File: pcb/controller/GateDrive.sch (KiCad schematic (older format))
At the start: 0 parts

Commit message: controller schematic capture almost done
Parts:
- added C? (x4): 10u, symbol Device:C
- added C? (x8): 0.1u, symbol Device:C
- added C? (x4): 1u, symbol Device:C
- added J? (x2): Conn_01x02_Female, symbol Connector:Conn_01x02_Female
- added Q? (x4): Q_NMOS_GSD, symbol Device:Q_NMOS_GSD
- added R? (x4): 10k, symbol Device:R
- added U? (x4): IXDD609D2, symbol wbraun_ic_lib:IXDD609D2
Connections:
- new net: C?.2, Q?.3 (D), R?.2, U?.3 (EN) (x4)
- new net: C?.2, C?.2, U?.6 (OUT), U?.7 (OUT) (x2)
- new net: J?.2 (Pin_2), U?.6 (OUT), U?.7 (OUT) (x2)
- new net: C?.1, C?.1, J?.1 (Pin_1) (x2)
- new net +24V: C?.1, C?.1, C?.1, C?.1, C?.1, C?.1, C?.1, C?.1, R?.1, R?.1, R?.1, R?.1, U?.1 (VCC), U?.1 (VCC), U?.1 (VCC), U?.1 (VCC), U?.8 (VCC), U?.8 (VCC), U?.8 (VCC), U?.8 (VCC)
- new net EN_1: Q?.1 (G)
- new net EN_2: Q?.1 (G)
- new net EN_3: Q?.1 (G)
- new net EN_4: Q?.1 (G)
- new net GATE_1: U?.2 (IN)
- new net GATE_2: U?.2 (IN)
- new net GATE_3: U?.2 (IN)
- new net GATE_4: U?.2 (IN)
- new net GND: C?.1, C?.1, C?.1, C?.1, C?.2, C?.2, C?.2, C?.2, C?.2, C?.2, C?.2, C?.2, Q?.2 (S), Q?.2 (S), Q?.2 (S), Q?.2 (S), U?.4 (GND), U?.4 (GND), U?.4 (GND), U?.4 (GND), U?.5 (GND), U?.5 (GND), U?.5 (GND), U?.5 (GND), U?.9 (EP), U?.9 (EP), U?.9 (EP), U?.9 (EP)

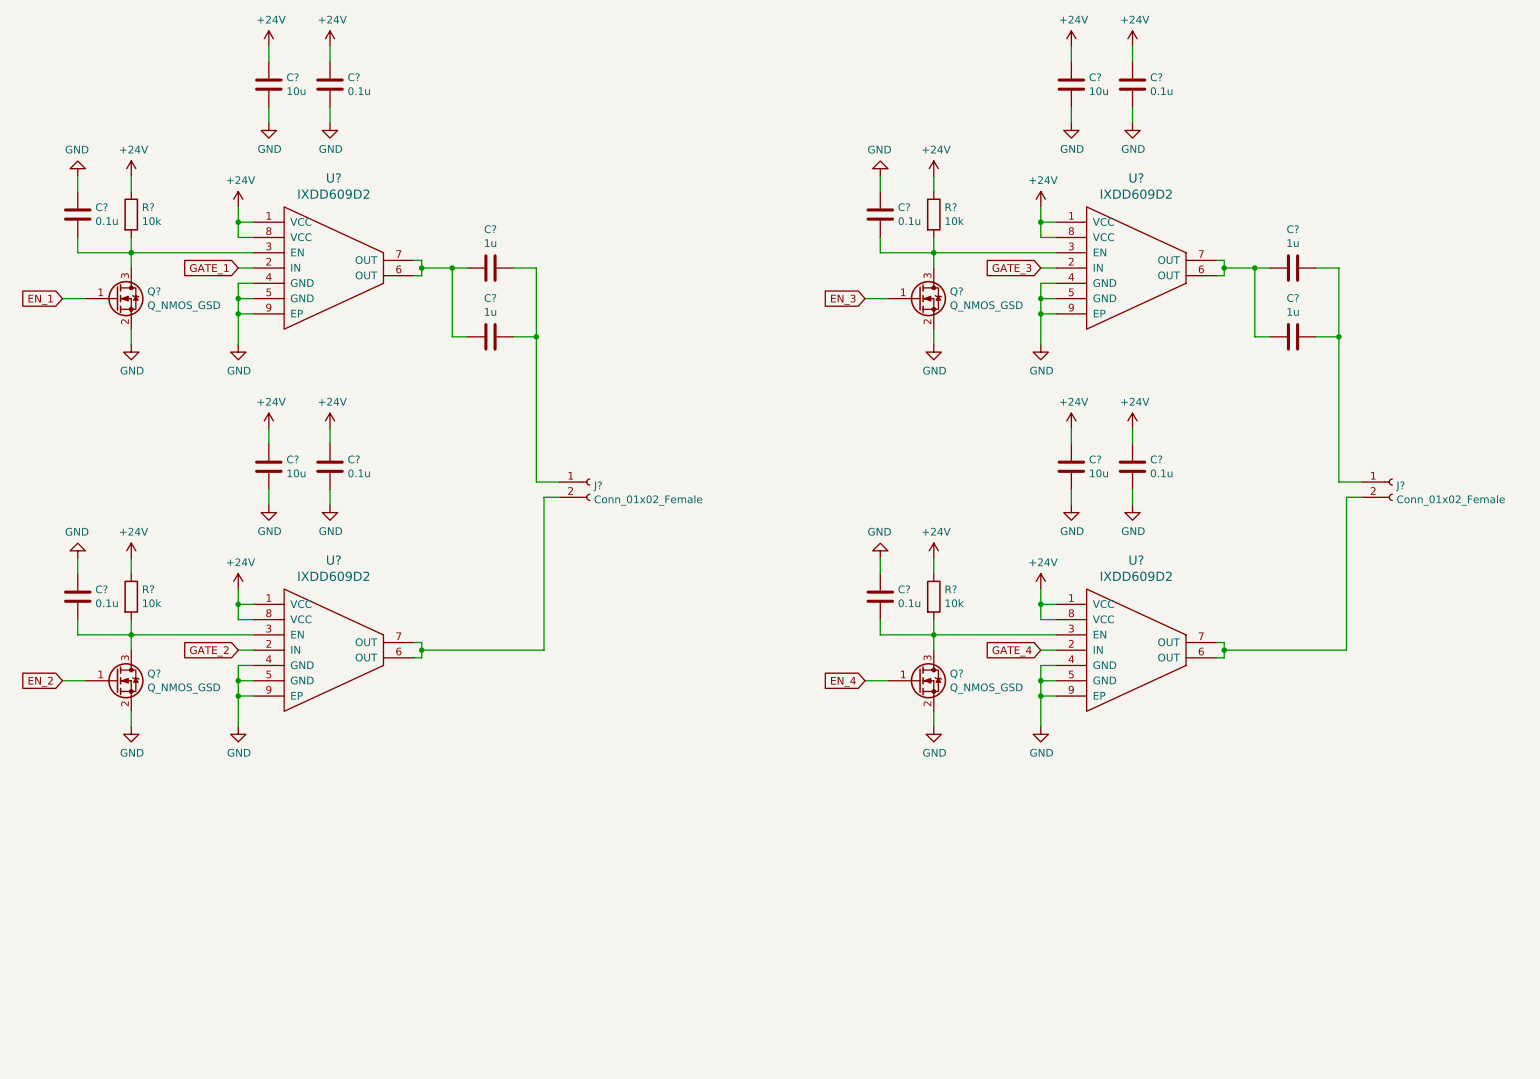
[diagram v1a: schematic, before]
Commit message: started assigning footprints
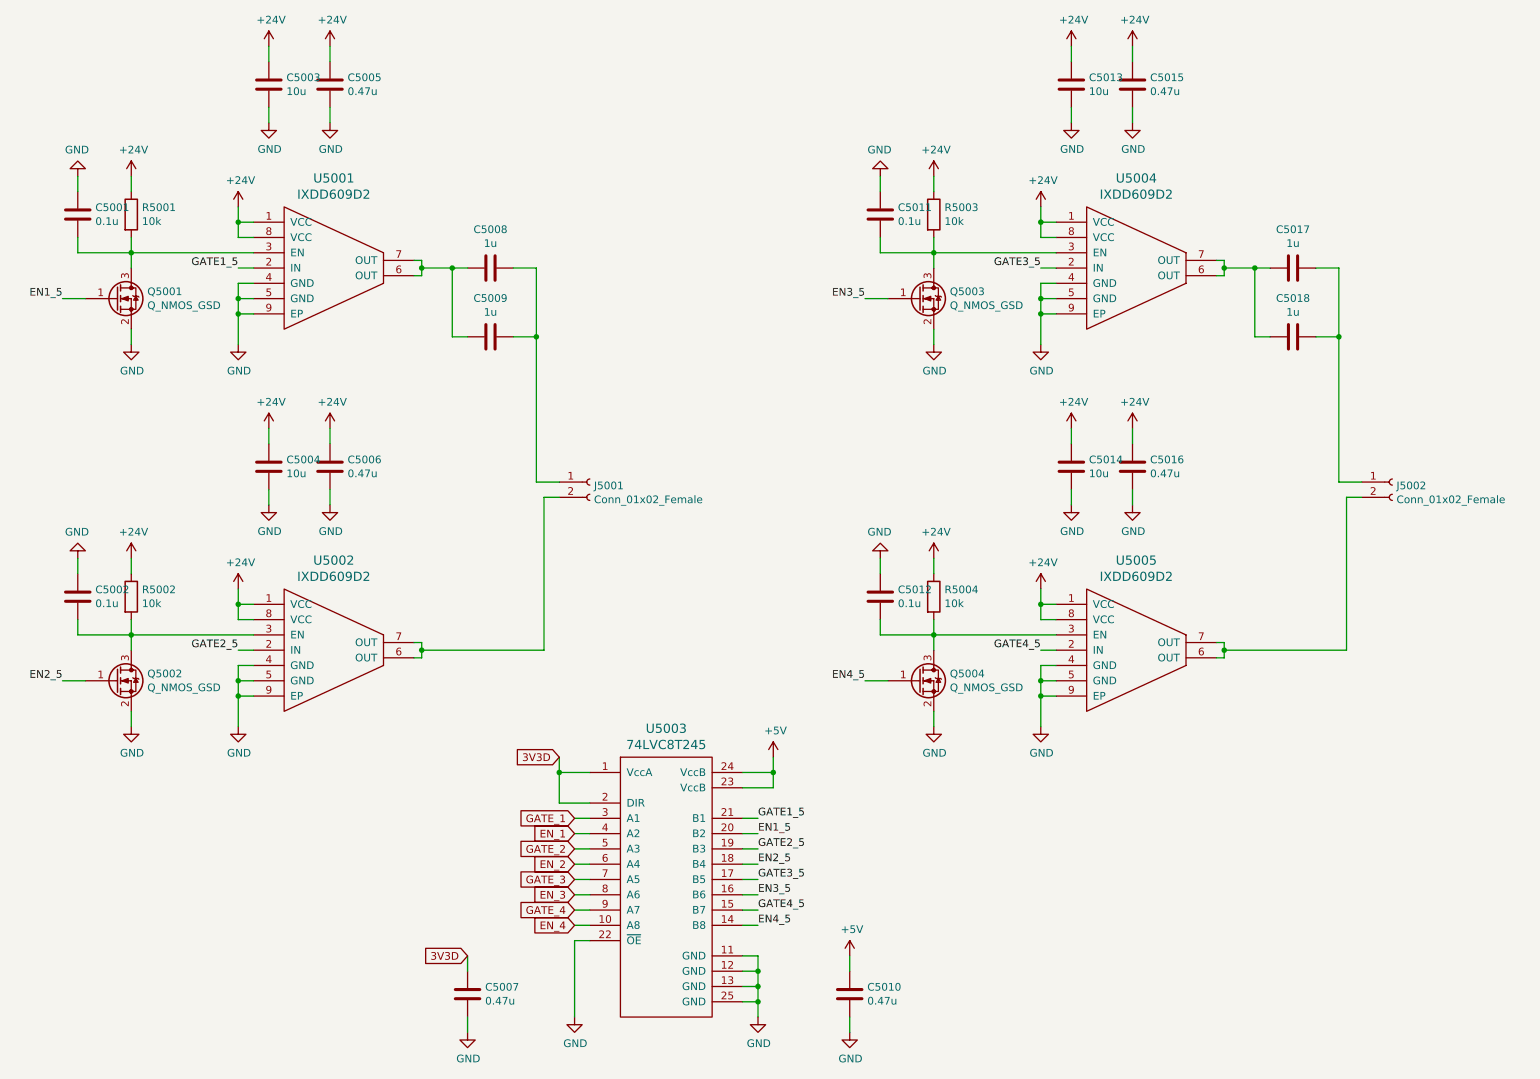
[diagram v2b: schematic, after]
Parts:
- added C5007, C5010: 0.47u, Capacitor_SMD:C_0402_1005Metric, symbol Device:C
- added U5003: 74LVC8T245, symbol wbraun_ic_lib:74LVC8T245
- C5001, C5002, C5008, C5009, C5011, C5012: renamed from C?; footprint (none) -> Capacitor_SMD:C_0805_2012Metric
- C5003, C5004, C5013: renamed from C?; footprint (none) -> Capacitor_SMD:C_1206_3216Metric
- C5005, C5006: renamed from C?; value 0.1u -> 0.47u; footprint (none) -> Capacitor_SMD:C_0805_2012Metric
- C5015, C5016: renamed from C?; value 0.1u -> 0.47u
- gave numbers to parts that had none: 17
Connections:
- net EN_1: now also U5003.4 (A2); no longer Q5001.1 (G)
- net EN_2: now also U5003.6 (A4); no longer Q5002.1 (G)
- net EN_3: now also U5003.8 (A6); no longer Q5003.1 (G)
- net EN_4: now also U5003.10 (A8); no longer Q5004.1 (G)
- net GATE_1: now also U5003.3 (A1); no longer U5001.2 (IN)
- net GATE_2: now also U5003.5 (A3); no longer U5002.2 (IN)
- net GATE_3: now also U5003.7 (A5); no longer U5004.2 (IN)
- net GATE_4: now also U5003.9 (A7); no longer U5005.2 (IN)
- net GND: now also C5007.2, C5010.2, U5003.11 (GND), U5003.12 (GND), U5003.13 (GND), U5003.22 (~OE), U5003.25 (GND)
- new net +5V: C5010.1, U5003.23 (VccB), U5003.24 (VccB)
- new net 3V3D: C5007.1, U5003.1 (VccA), U5003.2 (DIR)
- new net EN1_5: Q5001.1 (G), U5003.20 (B2)
- new net EN2_5: Q5002.1 (G), U5003.18 (B4)
- new net EN3_5: Q5003.1 (G), U5003.16 (B6)
- new net EN4_5: Q5004.1 (G), U5003.14 (B8)
- new net GATE1_5: U5001.2 (IN), U5003.21 (B1)
- new net GATE2_5: U5002.2 (IN), U5003.19 (B3)
- new net GATE3_5: U5003.17 (B5), U5004.2 (IN)
- new net GATE4_5: U5003.15 (B7), U5005.2 (IN)

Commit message: pcb component placement almost done
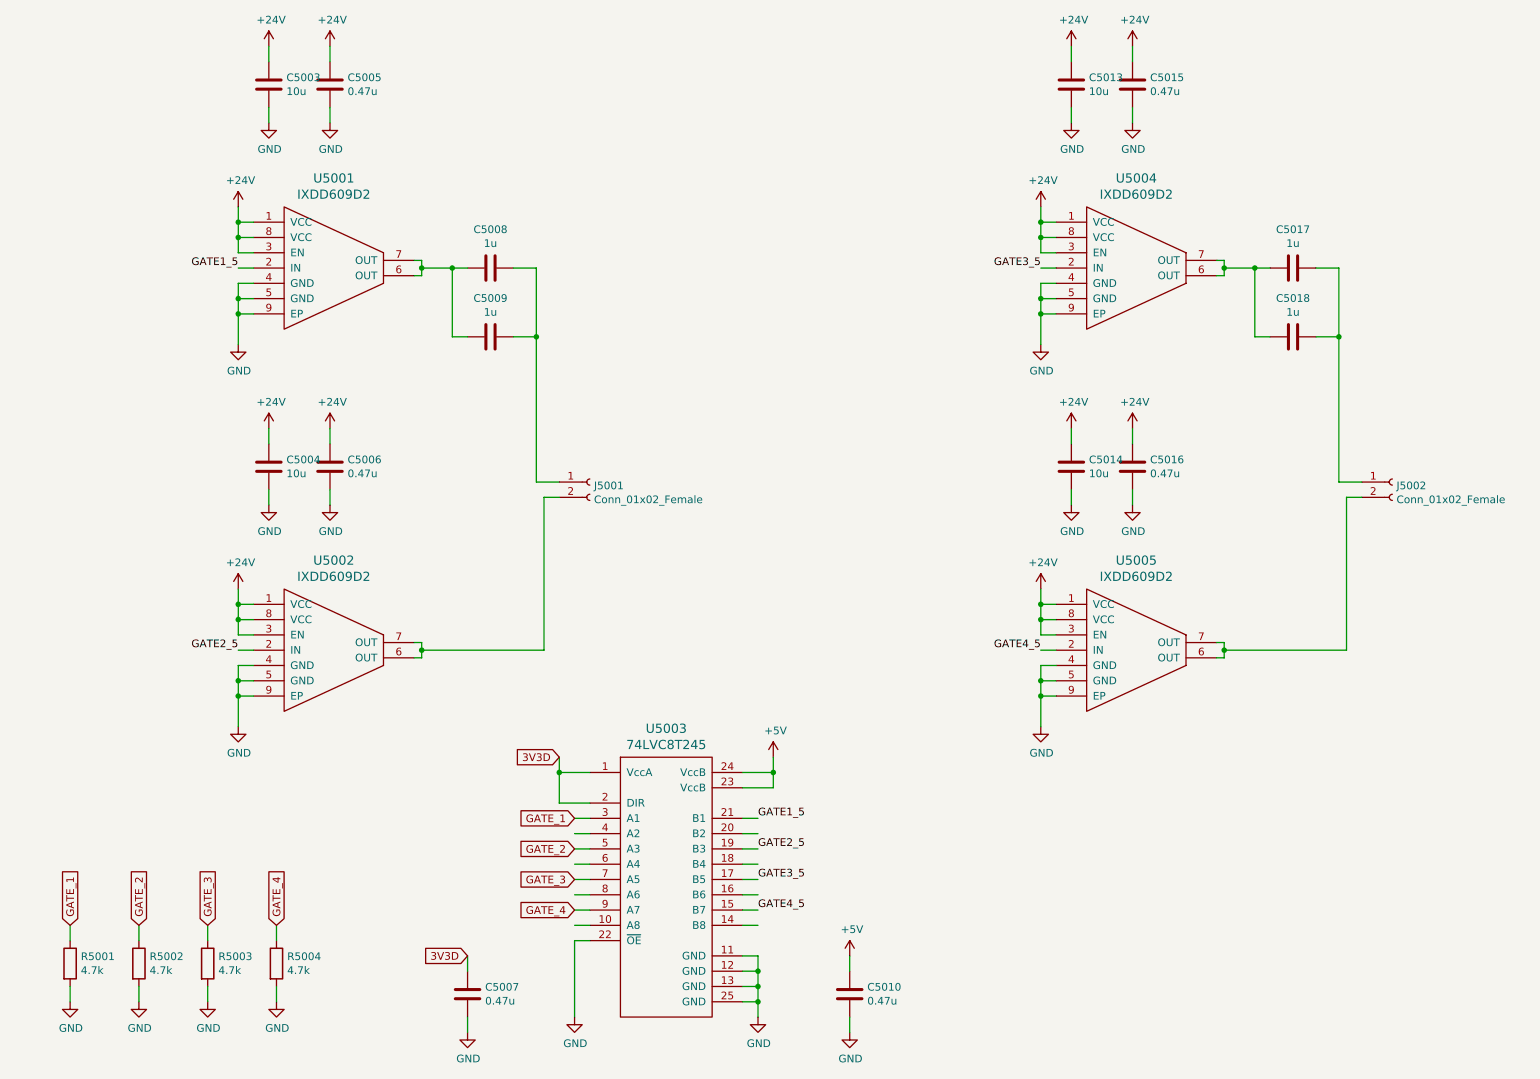
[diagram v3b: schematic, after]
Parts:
- removed C5001, C5002, C5011, C5012: 0.1u, Capacitor_SMD:C_0805_2012Metric, symbol Device:C
- removed Q5001, Q5002, Q5003, Q5004: Q_NMOS_GSD, symbol Device:Q_NMOS_GSD
- C5014, C5017, C5018: footprint (none) -> Capacitor_SMD:C_1206_3216Metric
- C5015, C5016: footprint (none) -> Capacitor_SMD:C_0805_2012Metric
- J5001, J5002: footprint (none) -> wbraun_smd:TerminalBlock-5.0mm-2
- R5001, R5002, R5003, R5004: value 10k -> 4.7k; footprint (none) -> Resistor_SMD:R_0402_1005Metric
- U5001, U5002, U5004, U5005: footprint (none) -> wbraun_smd:DFN-8_5x4mm_P0.95mm
- U5003: footprint (none) -> wbraun_smd:DHVQFN24_3.5x5.5mm_P0.5mm
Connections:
- net labels removed: EN1_5, EN2_5, EN3_5, EN4_5, EN_1, EN_2, EN_3, EN_4
- wire segments 174 -> 154

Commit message: controller PCB routing progress
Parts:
- J5001, J5002: footprint wbraun_smd:TerminalBlock-5.0mm-2 -> wbraun_smd:Terminal-block-plug_2x1_3.5mm-pitch
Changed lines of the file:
@@
 F 0 "J5001" H 4527 3876 50  0000 L CNN
 F 1 "Conn_01x02_Female" H 4527 3785 50  0000 L CNN
-F 2 "wbraun_smd:TerminalBlock-5.0mm-2" H 4500 3900 50  0001 C CNN
+F 2 "wbraun_smd:Terminal-block-plug_2x1_3.5mm-pitch" H 4500 3900 50  0001 C CNN
 F 3 "~" H 4500 3900 50  0001 C CNN
 	1    4500 3900
@@
 F 0 "J5002" H 9777 3876 50  0000 L CNN
 F 1 "Conn_01x02_Female" H 9777 3785 50  0000 L CNN
-F 2 "wbraun_smd:TerminalBlock-5.0mm-2" H 9750 3900 50  0001 C CNN
+F 2 "wbraun_smd:Terminal-block-plug_2x1_3.5mm-pitch" H 9750 3900 50  0001 C CNN
 F 3 "~" H 9750 3900 50  0001 C CNN
 	1    9750 3900

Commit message: routing almost done
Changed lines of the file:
@@
 Wire Wire Line
 	2300 5000 2200 5000
-Text GLabel 4400 6300 0    50   Input ~ 0
+Text GLabel 4400 6200 0    50   Input ~ 0
 GATE_2
 Wire Wire Line
@@
 Wire Wire Line
 	7550 2500 7450 2500
-Text GLabel 4400 6500 0    50   Input ~ 0
+Text GLabel 4400 6300 0    50   Input ~ 0
 GATE_3
 Wire Wire Line
@@
 Wire Wire Line
 	7550 5000 7450 5000
-Text GLabel 4400 6700 0    50   Input ~ 0
+Text GLabel 4400 6400 0    50   Input ~ 0
 GATE_4
 Wire Wire Line
@@
 	5500 6400 5600 6400
 Wire Wire Line
-	5500 6500 5600 6500
-Wire Wire Line
-	5500 6600 5600 6600
-Wire Wire Line
-	5500 6700 5600 6700
-Wire Wire Line
-	5500 6800 5600 6800
-Wire Wire Line
 	4500 6100 4400 6100
 Wire Wire Line
@@
 Text Label 5600 6100 0    50   ~ 0
 GATE1_5
+Text Label 5600 6200 0    50   ~ 0
+GATE2_5
 Text Label 5600 6300 0    50   ~ 0
-GATE2_5
-Text Label 5600 6500 0    50   ~ 0
 GATE3_5
-Text Label 5600 6700 0    50   ~ 0
+Text Label 5600 6400 0    50   ~ 0
 GATE4_5
 Text Label 2200 2500 2    50   ~ 0
@@
 Text GLabel 2450 6800 1    50   Input ~ 0
 GATE_4
+Wire Wire Line
+	4400 6500 4400 6600
+Connection ~ 4400 6900
+Connection ~ 4400 6600
+Wire Wire Line
+	4400 6600 4400 6700
+Connection ~ 4400 6700
+Wire Wire Line
+	4400 6700 4400 6800
+Connection ~ 4400 6800
+Wire Wire Line
+	4400 6800 4400 6900
 $EndSCHEMATC

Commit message: updated schematic component values
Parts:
- C5005, C5006, C5015, C5016: value 0.47u -> 1u
- C5008, C5017: value 1u -> 10u
- R5001, R5002, R5003, R5004: value 4.7k -> 470
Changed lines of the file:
@@
 P 2800 1300
 F 0 "C5005" H 2915 1346 50  0000 L CNN
-F 1 "0.47u" H 2915 1255 50  0000 L CNN
+F 1 "1u" H 2915 1255 50  0000 L CNN
 F 2 "Capacitor_SMD:C_0805_2012Metric" H 2838 1150 50  0001 C CNN
 F 3 "~" H 2800 1300 50  0001 C CNN
@@
 P 2800 3800
 F 0 "C5006" H 2915 3846 50  0000 L CNN
-F 1 "0.47u" H 2915 3755 50  0000 L CNN
+F 1 "1u" H 2915 3755 50  0000 L CNN
 F 2 "Capacitor_SMD:C_0805_2012Metric" H 2838 3650 50  0001 C CNN
 F 3 "~" H 2800 3800 50  0001 C CNN
@@
 P 3850 2500
 F 0 "C5008" V 3598 2500 50  0000 C CNN
-F 1 "1u" V 3689 2500 50  0000 C CNN
+F 1 "10u" V 3689 2500 50  0000 C CNN
 F 2 "Capacitor_SMD:C_0805_2012Metric" H 3888 2350 50  0001 C CNN
 F 3 "~" H 3850 2500 50  0001 C CNN
@@
 P 8050 1300
 F 0 "C5015" H 8165 1346 50  0000 L CNN
-F 1 "0.47u" H 8165 1255 50  0000 L CNN
+F 1 "1u" H 8165 1255 50  0000 L CNN
 F 2 "Capacitor_SMD:C_0805_2012Metric" H 8088 1150 50  0001 C CNN
 F 3 "~" H 8050 1300 50  0001 C CNN
@@
 P 8050 3800
 F 0 "C5016" H 8165 3846 50  0000 L CNN
-F 1 "0.47u" H 8165 3755 50  0000 L CNN
+F 1 "1u" H 8165 3755 50  0000 L CNN
 F 2 "Capacitor_SMD:C_0805_2012Metric" H 8088 3650 50  0001 C CNN
 F 3 "~" H 8050 3800 50  0001 C CNN
@@
 P 9100 2500
 F 0 "C5017" V 8848 2500 50  0000 C CNN
-F 1 "1u" V 8939 2500 50  0000 C CNN
+F 1 "10u" V 8939 2500 50  0000 C CNN
 F 2 "Capacitor_SMD:C_1206_3216Metric" H 9138 2350 50  0001 C CNN
 F 3 "~" H 9100 2500 50  0001 C CNN
@@
 P 1100 7050
 F 0 "R5001" H 1170 7096 50  0000 L CNN
-F 1 "4.7k" H 1170 7005 50  0000 L CNN
+F 1 "470" H 1170 7005 50  0000 L CNN
 F 2 "Resistor_SMD:R_0402_1005Metric" V 1030 7050 50  0001 C CNN
 F 3 "~" H 1100 7050 50  0001 C CNN
@@
 P 1550 7050
 F 0 "R5002" H 1620 7096 50  0000 L CNN
-F 1 "4.7k" H 1620 7005 50  0000 L CNN
+F 1 "470" H 1620 7005 50  0000 L CNN
 F 2 "Resistor_SMD:R_0402_1005Metric" V 1480 7050 50  0001 C CNN
 F 3 "~" H 1550 7050 50  0001 C CNN
@@
 P 2000 7050
 F 0 "R5003" H 2070 7096 50  0000 L CNN
-F 1 "4.7k" H 2070 7005 50  0000 L CNN
+F 1 "470" H 2070 7005 50  0000 L CNN
 F 2 "Resistor_SMD:R_0402_1005Metric" V 1930 7050 50  0001 C CNN
 F 3 "~" H 2000 7050 50  0001 C CNN
@@
 P 2450 7050
 F 0 "R5004" H 2520 7096 50  0000 L CNN
-F 1 "4.7k" H 2520 7005 50  0000 L CNN
+F 1 "470" H 2520 7005 50  0000 L CNN
 F 2 "Resistor_SMD:R_0402_1005Metric" V 2380 7050 50  0001 C CNN
 F 3 "~" H 2450 7050 50  0001 C CNN
